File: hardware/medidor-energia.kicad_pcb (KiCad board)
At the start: 2 copper layers, 150 x 90 mm, 56 parts, among them J1 Bornera 5 V, J2 Jack 3,5 mm de panel (pinza S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, J3 Jack 3,5 mm de panel (pinza S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, J5 Bornera ZMPT, J6 LCD (VCC GND DIN CS DC BL CLK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, J7 Reserva ADC1, SW1 Pulsador de panel 12 mm NA, SW2 Pulsador de panel 12 mm NA, U1 ESP32-DevKitC V4 (38 pines)

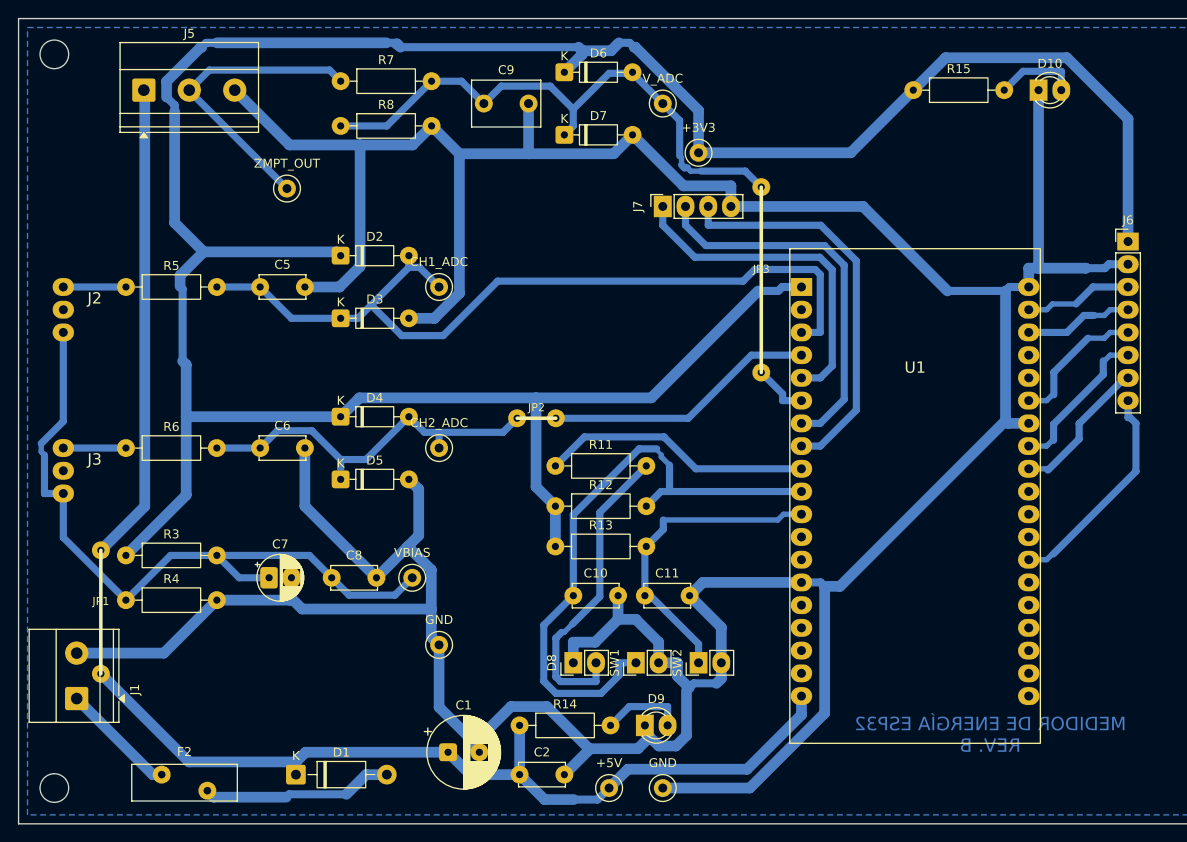
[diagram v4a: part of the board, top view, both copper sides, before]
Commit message: Correcciones de la revisión del diseño
- Firmware: la adquisición la despierta un temporizador de hardware (antes esperaba de forma activa
  y bloqueaba el arranque); eventos de Wi-Fi en el núcleo 0; tarea de adquisición creada al final.
- Fase: historia de tensión de 8 muestras, corrección de −8° a +11° con fase del ZMPT101B y de cada
  pinza; calibración guardada en NVS desde la consola serie (comando cal).
- Ventanas por cantidad de muestras cuando no hay cruces por cero (ZMPT101B desconectado).
- Hardware: C5 y C6 vuelven a VBIAS (antes a GND, acoplaban los canales ~1 %); PCB re-ruteada con
  2 puentes; placa perforada y simulación actualizadas.
- README: aislamiento del ZMPT101B y criterio de 100 MΩ, alimentación por USB, tierra, prueba de
  cortocircuito, calibración de fase y nuevas pruebas del cálculo.
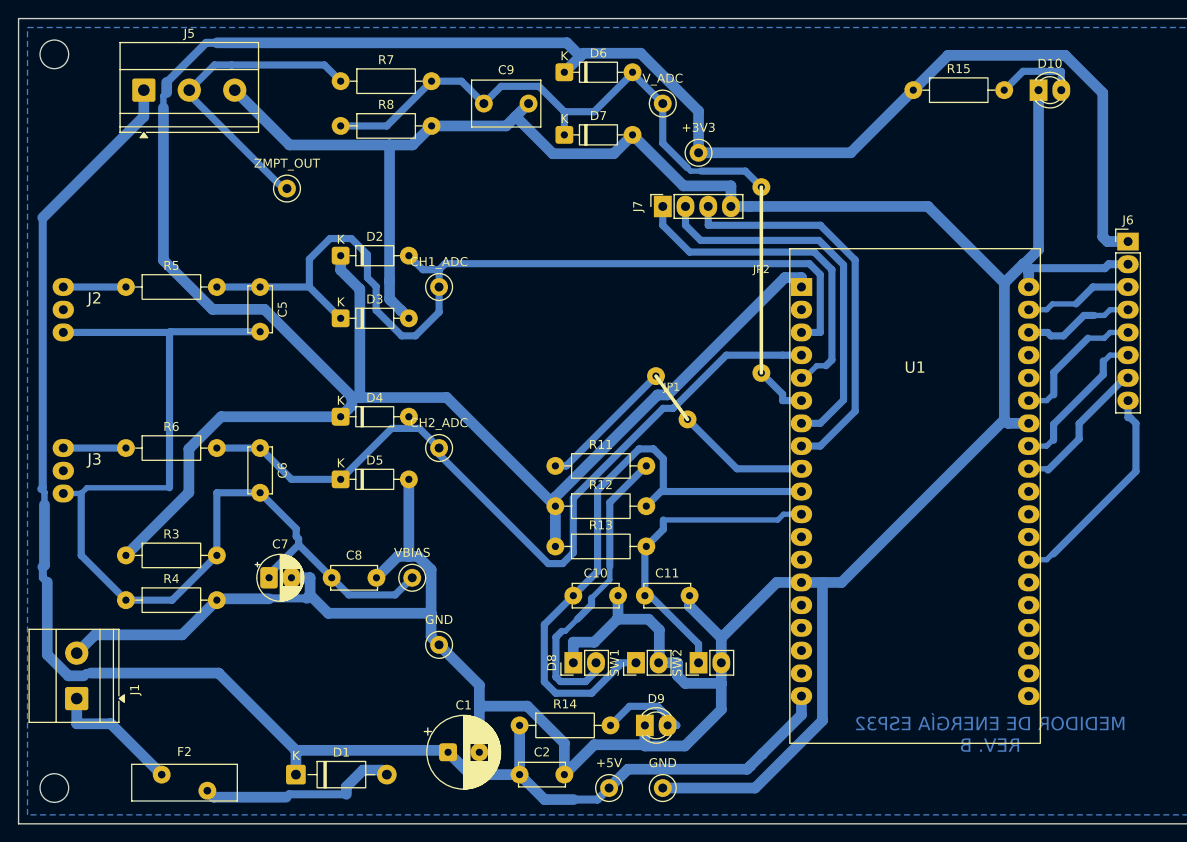
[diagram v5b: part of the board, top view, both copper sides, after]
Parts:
- removed JP3: puente, Medidor:Puente_alambre
- moved JP1 65.0 mm to (96.2, 65.0)
- moved JP2 37.6 mm to (108.0, 43.8)
- turned C5 to -90 degrees
- turned C6 to -90 degrees
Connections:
- C5 pad 2: GND -> /VBIAS
- C6 pad 2: GND -> /VBIAS
- JP1 pad 1: +5V -> /LED_EST
- JP2 pad 1: /CH2_ADC -> /V_ADC
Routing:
- net GND: track 463.1 -> 423.1 mm
- net /VBIAS: track 79.7 -> 118.1 mm
- net +5V: track 151.5 -> 173.8 mm
- net /CH2_ADC: track 73.4 -> 90.4 mm
- net /CH1_ADC: track 94.3 -> 103.3 mm
- net +3V3: track 308.6 -> 314.6 mm
- net Net-(J1-Pin_1): track 13.0 -> 14.7 mm
- net /SW1: track 68.8 -> 67.7 mm
- net Net-(D1-A): track 21.4 -> 22.3 mm
- net Net-(D9-A): track 9.35 -> 10.2 mm
- net /V_ADC: track 71.3 -> 70.6 mm
- net /ZMPT_OUT: track 33.9 -> 34.6 mm
- net Net-(D8-A): track 34.7 -> 34.1 mm

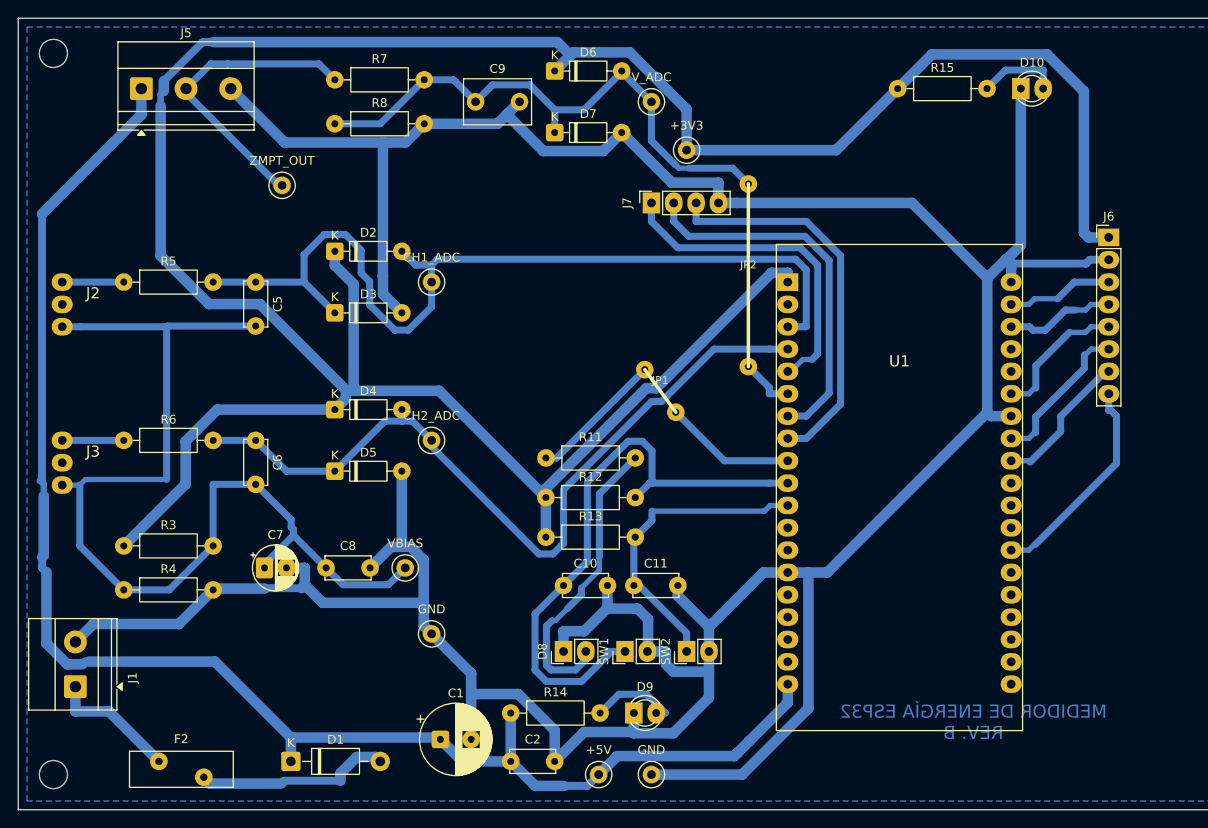
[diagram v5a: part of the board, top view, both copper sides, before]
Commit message: PCB con las reglas del taller de CNC: pistas de 0,9 mm y 1 mm de separación
- Pads de las filas de 2,54 mm a 1,5 × 2,4 mm para dejar 1 mm entre pads vecinos.
- Freerouting sin adelgazar pistas en los pines y con 1,1 mm de separación de ruteo.
- 10 puentes de alambre; DRC sin errores con mínimos de 1,0 mm y 0,9 mm en el proyecto.
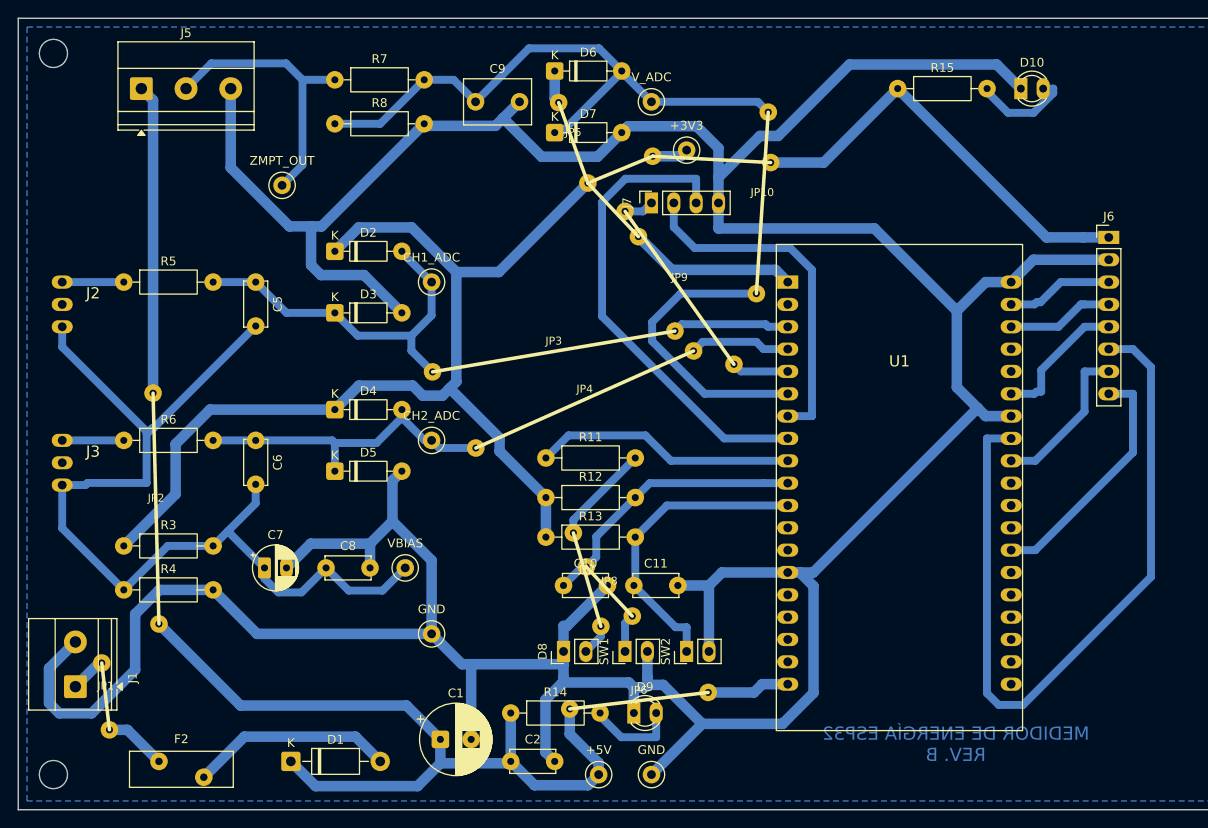
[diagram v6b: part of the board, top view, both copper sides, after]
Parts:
- added JP10: puente, Medidor:Puente_alambre, F.Cu at (108.9, 56.3)
- added JP3: puente, Medidor:Puente_alambre, F.Cu at (72.1, 65.2)
- added JP4: puente, Medidor:Puente_alambre, F.Cu at (77.0, 73.9)
- added JP5: puente, Medidor:Puente_alambre, F.Cu at (86.5, 34.6)
- added JP6: puente, Medidor:Puente_alambre, F.Cu at (87.7, 103.5)
- added JP7: puente, Medidor:Puente_alambre, F.Cu at (88.1, 83.5)
- added JP8: puente, Medidor:Puente_alambre, F.Cu at (89.6, 87.4)
- added JP9: puente, Medidor:Puente_alambre, F.Cu at (94.0, 47.0)
- moved JP2 71.7 mm to (40.3, 67.6)
- moved JP1 70.2 mm to (34.5, 98.3)
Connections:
- JP1 pad 1: /LED_EST -> Net-(J1-Pin_1)
- JP2 pad 1: /V_ADC -> +5V
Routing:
- net +3V3: track 314.6 -> 195.9 mm
- net /LCD_BL: track 17.3 -> 86.5 mm
- net GND: track 423.1 -> 474.7 mm
- net /CH1_ADC: track 103.3 -> 55.4 mm
- net /CH2_ADC: track 90.4 -> 48.2 mm
- net +5V: track 173.8 -> 138.1 mm
- net /SW1: track 67.7 -> 36.0 mm
- net /V_ADC: track 70.6 -> 101.7 mm
- net /RES_IO34: track 37.4 -> 9.87 mm
- net Net-(D8-A): track 34.1 -> 15.0 mm
- net /RES_IO33: track 44.6 -> 54.4 mm
- net /VBIAS: track 118.1 -> 111.9 mm
- net Net-(J1-Pin_1): track 14.7 -> 11.2 mm
- net /LCD_RST: track 24.5 -> 27.9 mm
- net /ZMPT_OUT: track 34.6 -> 31.8 mm
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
